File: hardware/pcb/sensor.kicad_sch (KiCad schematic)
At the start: 23 parts, among them SW1 Left click, SW2 Right Click, SW3 Middle click, U100 LDO 1V8, U2 PMW3360

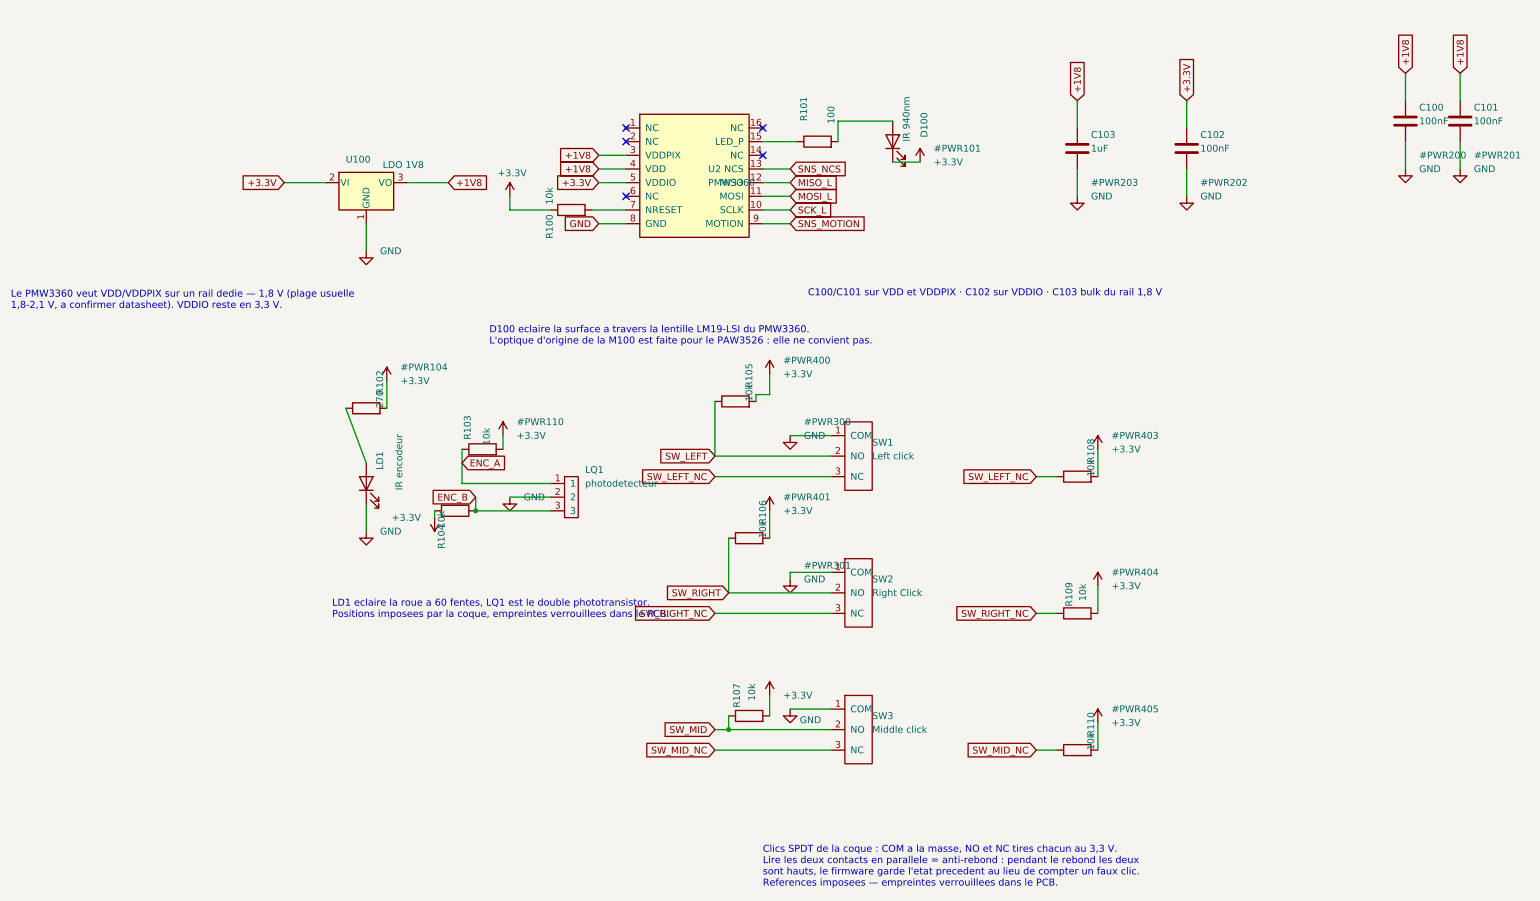
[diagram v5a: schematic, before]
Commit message: schema REV2 : LQ1 recable, D100 supprimee, VBAT_SENSE sur ADC1, U100 corrige
LQ1 etait cable a l'envers depuis le portage du fork USB-Mouse. Le symbole
Optical_Mouse:LQ ne nommait ses broches que "1, 2, 3", sans fonction, et le
portage a suppose un double phototransistor A/COM/B. Le schema d'origine de la
M100 dit autre chose : broche 1 = DATA, 2 = VCC, 3 = GND.

La carte alimentait donc le capteur a l'envers — son VCC a la masse, sa masse
tiree au 3,3 V par R104. Le courant passait par la diode de substrat interne et
clampait les deux nets a 0,65 V, insensible a la lumiere comme au pilotage.
Deux LQ1 ont ete dessoudes avant que la confrontation au schema source ne donne
la reponse.

  - LQ1.2 -> +3V3, LQ1.3 -> GND, LQ1.1 (DATA) reste sur ENC_A / GPIO7
  - LD1 cathode -> R102 -> GPIO9, renomme ENC_LED : la LED de molette devient
    pilotable, comme sur la M100 d'origine. Gain d'autonomie, et un diagnostic
    qui aurait pris une minute au lieu d'une journee.
  - R102 = 820 ohms : 2,6 mA, le point de fonctionnement d'origine transpose
    du 5 V USB au 3,3 V
  - R104 = 0 ohm (pont vers la masse), R103 conservee
  - symbole LQ : broches nommees DATA / VCC / GND, dans le cache et dans
    optical_mouse.lib, pour que l'erreur soit impossible a refaire

D100 supprimee : le PMW3389 embarque sa LED IR (broche 15 LED_P = anode). La
LED externe etait de surcroit montee a l'envers et bloquait le courant, rendant
le capteur aveugle. R101 = 16 ohms alimentee depuis le rail capteur, renomme
+1V8 -> +2V0.

VBAT_SENSE passe de U6.21 (GPIO13, ADC2_CH2) a U6.12 (GPIO8, ADC1_CH7) :
l'ADC2 de l'ESP32-S3 est partage avec le driver WiFi.

U100 : les numeros de pad du symbole sont corriges — VI porte le pad 3 et VO le
pad 2, soit le brochage reel du XC6206 en SOT-23. Le schema cesse de mentir et
la netlist devient juste d'elle-meme.

Co-Authored-By: Claude Opus 5 (1M context) <noreply@anthropic.com>
Claude-Session: https://claude.ai/code/session_01VhxWZJVUd4SHAcp3eUFVJV
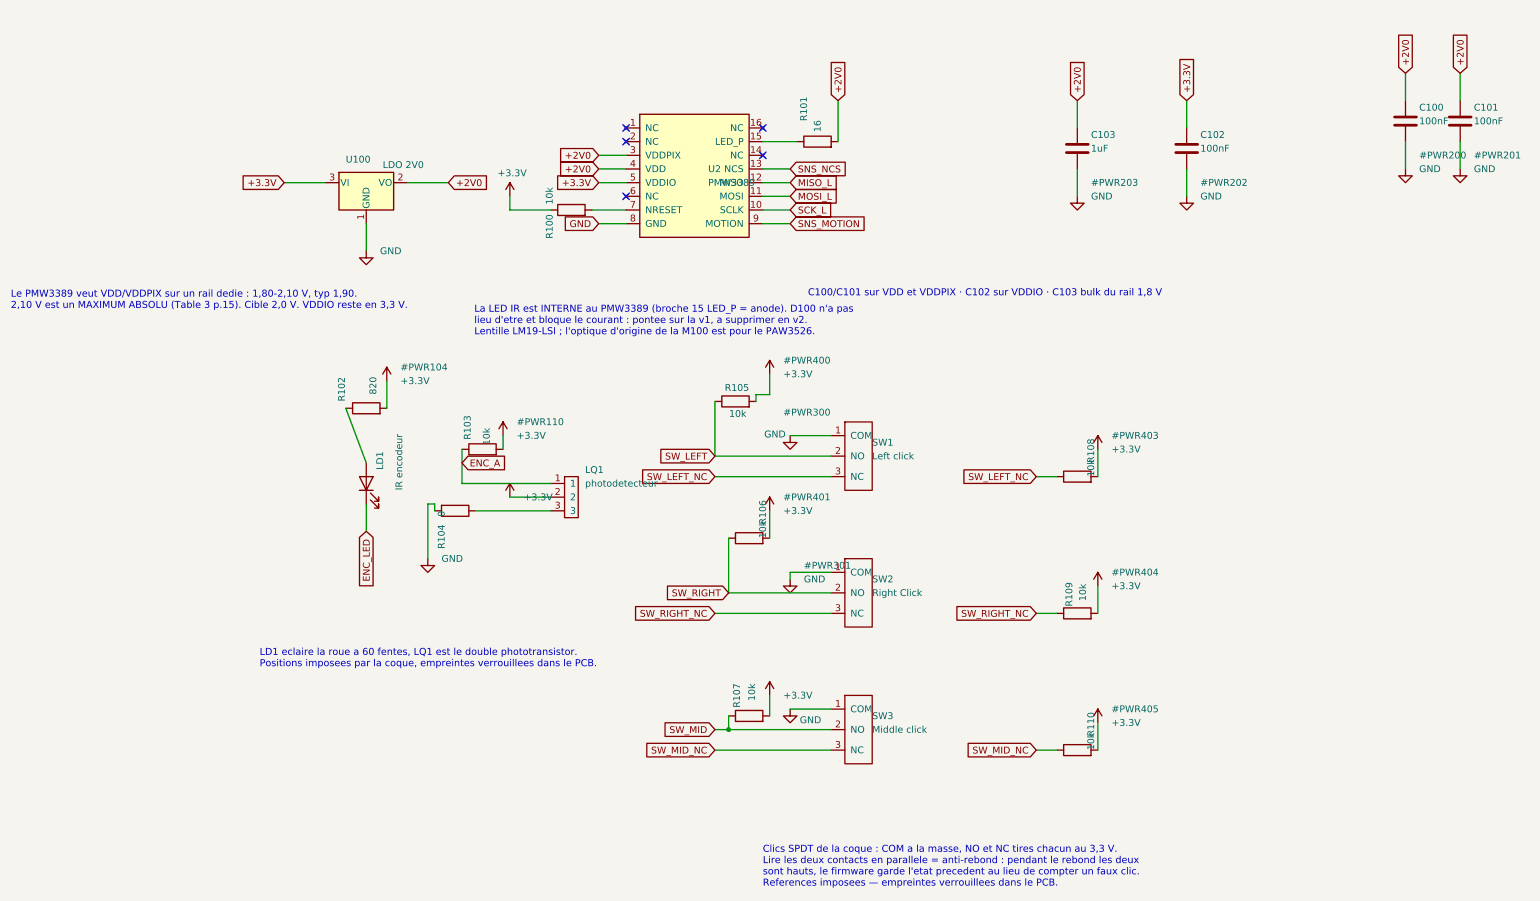
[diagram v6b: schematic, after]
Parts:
- removed D100: IR 940nm, LED_SMD:LED_0805_2012Metric, symbol Device:LED
- R101: value 100 -> 16
- R102: value 270 -> 820
- R104: value 10k -> 0
- U100: value LDO 1V8 -> LDO 2V0
- U2: value PMW3360 -> PMW3389
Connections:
- net +3.3V: now also LQ1.2, U100.3 (VI); no longer R104.2, U100.2 (VI)
- net GND: now also R104.2; no longer LD1.1 (K), LQ1.2
- net +2V0: now reaches R101.2
- net +2V0: now also C100.1, C101.1, C103.1, U100.2 (VO), U2.3 (VDDPIX), U2.4 (VDD)
- removed net +1V8: C100.1, C101.1, C103.1, U100.3 (VO), U2.3 (VDDPIX), U2.4 (VDD)
- net ENC_B: no longer names the net of LQ1.3, R104.1
- new net ENC_LED: LD1.1 (K)
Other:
- note added: "La LED IR est INTERNE au PMW3389 (broche 15 LED_P = anode). D100 n'a pas lieu d'etre et bloque le courant : pontee sur la v1, a supprimer en v2. Lentille LM19-LSI ; l'optique d'origine de la M100 est pour le PAW3526."
- note added: "Le PMW3389 veut VDD/VDDPIX sur un rail dedie : 1,80-2,10 V, typ 1,90. 2,10 V est un MAXIMUM ABSOLU (Table 3 p.15). Cible 2,0 V. VDDIO reste en 3,3 V."
- note removed: "D100 eclaire la surface a travers la lentille LM19-LSI du PMW3360. L'optique d'origine de la M100 est faite pour le PAW3526 : elle ne convient pas."
- note removed: "Le PMW3360 veut VDD/VDDPIX sur un rail dedie — 1,8 V (plage usuelle 1,8-2,1 V, a confirmer datasheet). VDDIO reste en 3,3 V."
